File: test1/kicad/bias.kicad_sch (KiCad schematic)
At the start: 12 parts, among them Q40 PMZ1200UPEYL, Q41 PMZ1200UPEYL, Q42 2N7002 DNP, Q43 2N7002 DNP, U40 MCP4728, U41 OPA2388

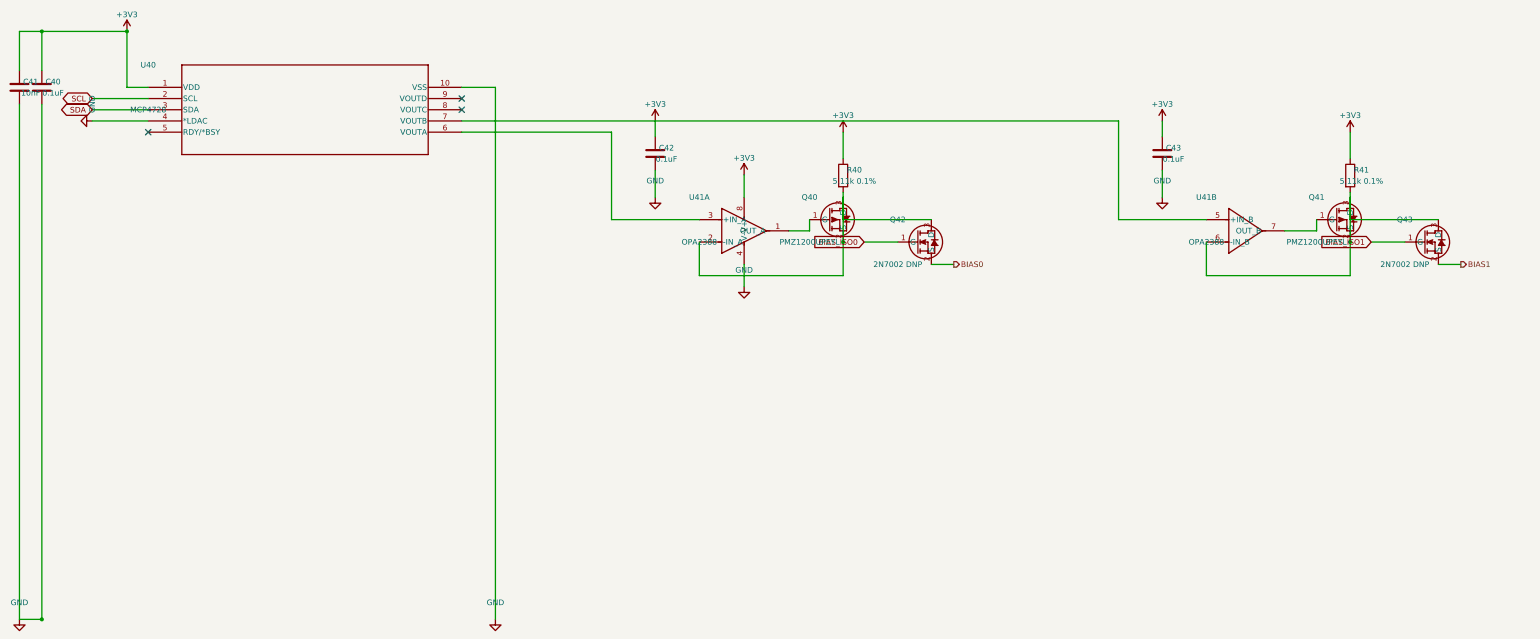
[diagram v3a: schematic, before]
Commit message: Split test1 generator into per-sheet package with netlist YAML + strict validator
Combines three layered changes:

1. Apply the design-review audit (test1/error_log.md): 9 ERRORs + 10
   WARNINGs from the new .claude/skills/design_review.md skill — FMC
   LA-bank 0Ω routing, Bobcat SPI/control/GPIO pull network, LDO
   ANY-OUT to FPGA, LDO_PG pull-up + series, bias DNP convention,
   kelvin SNS, per-pin VDDIO + bulk caps, BIAS bypass, VADJ/VDDIO bulk,
   MCP4728 EEPROM provisioning notes, shared-rail decision documented.

2. Refactor test1/gen_schematic.py (1825 lines → 138-line entry point)
   into a per-sheet package at test1/gen/:
     config.py / symbols.py / shared.py  — primitives, Sheet container,
     LA_ASSIGN, footprints, sexpr emit
     build_<sheet>.py × 7                — one builder per child sheet
     netlist.py / validator.py           — YAML loader + strict checker
   Per-session context for any single sheet drops to ~500 lines.
   Also sorts non-deterministic set iteration that made fmc.kicad_sch
   diff noisily across runs.

3. Add a declarative connectivity layer (netlist/<sheet>.yaml):
   parts inventory + nets (power / hier / global / internal), with
   explicit unit syntax for multi-unit symbols (U41:u2.7, J3:u3.G16).
   The strict validator runs at the end of every build_<sheet>() call:
     - inventory: YAML parts ↔ placed (refdes, unit) parity
     - connectivity: every YAML net member is in a connected component
       named the YAML net name (Union-Find on wires + junctions + label
       anchors + power-symbol pins; T-intersections auto-connect)
     - internal nets: members in one component, no name check
   Sheet now records structured PlacedPart/wire/label data alongside
   the s-expr emit; validator reads those instead of re-parsing.

All 6 child sheets' .kicad_sch outputs are byte-identical to the
post-design-review reference, and verify_project.py reports 0 issues.

Co-Authored-By: Claude Opus 4.7 (1M context) <noreply@anthropic.c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
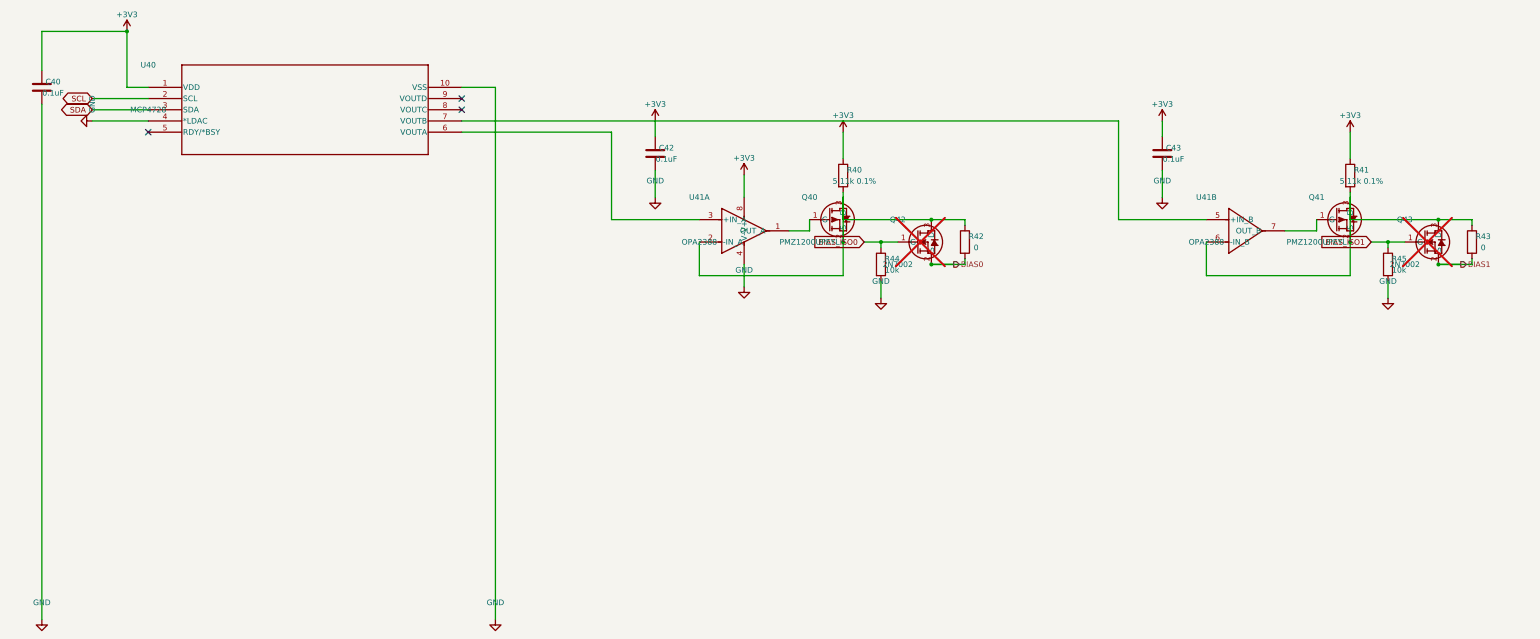
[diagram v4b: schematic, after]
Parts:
- removed C41: 10nF, Capacitor_SMD:C_0402_1005Metric, symbol Device:C
- added R42, R43: 0, Resistor_SMD:R_0402_1005Metric, symbol Device:R
- added R44, R45: 10k, Resistor_SMD:R_0402_1005Metric, symbol Device:R
- Q42, Q43: value 2N7002 DNP -> 2N7002; now not fitted
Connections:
- net BIAS0: now also R42.2
- net BIAS1: now also R43.2
- net BIAS_ISO0: now also R44.1
- net BIAS_ISO1: now also R45.1
- net GND: now also R44.2, R45.2
- net at Q41.2 (S), Q41.3 (D), Q43.3 (D)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: now also R43.1
- net at Q40.2 (S), Q40.3 (D), Q42.3 (D)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: now also R42.1
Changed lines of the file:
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@@
   (wire (pts (xy 55.88 83.81) (xy 55.88 200.66)) (stroke (width 0) (type default)))
   (symbol
-    (lib_id "Device:C")
-    (at 50.8 80 0)
-    (unit 1) (in_bom yes) (on_board yes) (dnp no)
-    (property "Reference" "C41" (at 53.339999999999996 78.73 0) (effects (font (size 1.27 1.27))))
-    (property "Value" "10nF" (at 53.339999999999996 81.27 0) (effects (font (size 1.27 1.27))))
-    (property "Footprint" "Capacitor_SMD:C_0402_1005Metric" (at 0 0 0) (effects (font (size 1.27 1.27)) (hide yes)))
-    (property "Datasheet" "" (at 0 0 0) (effects (font (size 1.27 1.27)) (hide yes)))
-    (pin "1")
-    (pin "2")
-    (instances
-      (project "test1"
-        (path "/4ed7a046-ef33-57d9-8730-321c05965af3/ddf1c49f-55ac-530a-9ee4-38ad9d14caf8" (reference "C41") (unit 1)))))
-  (wire (pts (xy 50.8 76.19) (xy 50.8 67.31)) (stroke (width 0) (type default)))
-  (wire (pts (xy 50.8 67.31) (xy 55.88 67.31)) (stroke (width 0) (type default)))
-  (junction (at 55.88 67.31) (diameter 0) (color 0 0 0 0))
-  (wire (pts (xy 50.8 83.81) (xy 50.8 200.66)) (stroke (width 0) (type default)))
-  (wire (pts (xy 50.8 200.66) (xy 55.88 200.66)) (stroke (width 0) (type default)))
-  (junction (at 55.88 200.66) (diameter 0) (color 0 0 0 0))
-  (symbol
-    (lib_id "power:GND")
-    (at 50.8 200.66 0)
-    (unit 1) (in_bom yes) (on_board yes) (dnp no)
-    (property "Reference" "#PWRa06f21d9" (at 50.8 194.31 0) (effects (font (size 1.27 1.27)) (hide yes)))
-    (property "Value" "GND" (at 50.8 196.85 0) (effects (font (size 1.27 1.27))))
-    (property "Footprint" "" (at 0 0 0) (effects (font (size 1.27 1.27)) (hide yes)))
-    (property "Datasheet" "" (at 0 0 0) (effects (font (size 1.27 1.27)) (hide yes)))
-    (pin "1")
-    (instances
-      (project "test1"
-        (path "/4ed7a046-ef33-57d9-8730-321c05965af3/ddf1c49f-55ac-530a-9ee4-38ad9d14caf8" (reference "#PWRa06f21d9") (unit 1)))))
+    (lib_id "power:GND")
+    (at 55.88 200.66 0)
+    (unit 1) (in_bom yes) (on_board yes) (dnp no)
+    (property "Reference" "#PWR807a04e0" (at 55.88 194.31 0) (effects (font (size 1.27 1.27)) (hide yes)))
+    (property "Value" "GND" (at 55.88 196.85 0) (effects (font (size 1.27 1.27))))
+    (property "Footprint" "" (at 0 0 0) (effects (font (size 1.27 1.27)) (hide yes)))
+    (property "Datasheet" "" (at 0 0 0) (effects (font (size 1.27 1.27)) (hide yes)))
+    (pin "1")
+    (instances
+      (project "test1"
+        (path "/4ed7a046-ef33-57d9-8730-321c05965af3/ddf1c49f-55ac-530a-9ee4-38ad9d14caf8" (reference "#PWR807a04e0") (unit 1)))))
   (symbol
     (lib_id "Lib:OPA2388")
@@
     (lib_id "Lib:2N7002")
     (at 250 115.08 0)
-    (unit 1) (in_bom yes) (on_board yes) (dnp no)
+    (unit 1) (in_bom yes) (on_board yes) (dnp yes)
     (property "Reference" "Q42" (at 250 110.0 0) (effects (font (size 1.27 1.27))))
-    (property "Value" "2N7002 DNP" (at 250 120.16 0) (effects (font (size 1.27 1.27))))
+    (property "Value" "2N7002" (at 250 120.16 0) (effects (font (size 1.27 1.27))))
     (property "Footprint" "Package_TO_SOT_SMD:SOT-23" (at 0 0 0) (effects (font (size 1.27 1.27)) (hide yes)))
     (property "Datasheet" "" (at 0 0 0) (effects (font (size 1.27 1.27)) (hide yes)))
@@
   (wire (pts (xy 250.0 115.08) (xy 242.38 115.08)) (stroke (width 0) (type default)))
   (global_label "BIAS_ISO0" (shape input) (at 242.38 115.08 180) (effects (font (size 1.27 1.27)) (justify right)))
+  (symbol
+    (lib_id "Device:R")
+    (at 265.24 115.08 0)
+    (unit 1) (in_bom yes) (on_board yes) (dnp no)
+    (property "Reference" "R42" (at 267.78000000000003 113.81 0) (effects (font (size 1.27 1.27))))
+    (property "Value" "0" (at 267.78000000000003 116.35 0) (effects (font (size 1.27 1.27))))
+    (property "Footprint" "Resistor_SMD:R_0402_1005Metric" (at 0 0 0) (effects (font (size 1.27 1.27)) (hide yes)))
+    (property "Datasheet" "" (at 0 0 0) (effects (font (size 1.27 1.27)) (hide yes)))
+    (pin "1")
+    (pin "2")
+    (instances
+      (project "test1"
+        (path "/4ed7a046-ef33-57d9-8730-321c05965af3/ddf1c49f-55ac-530a-9ee4-38ad9d14caf8" (reference "R42") (unit 1)))))
+  (junction (at 257.62 110.0) (diameter 0) (color 0 0 0 0))
+  (wire (pts (xy 257.62 110.0) (xy 265.24 110.0)) (stroke (width 0) (type default)))
+  (wire (pts (xy 265.24 110.0) (xy 265.24 111.27)) (stroke (width 0) (type default)))
+  (junction (at 257.62 120.16) (diameter 0) (color 0 0 0 0))
+  (wire (pts (xy 257.62 120.16) (xy 265.24 120.16)) (stroke (width 0) (type default)))
+  (wire (pts (xy 265.24 120.16) (xy 265.24 118.89)) (stroke (width 0) (type default)))
+  (junction (at 246.19 115.08) (diameter 0) (color 0 0 0 0))
+  (symbol
+    (lib_id "Device:R")
+    (at 246.19 120.16 0)
+    (unit 1) (in_bom yes) (on_board yes) (dnp no)
+    (property "Reference" "R44" (at 248.73 118.89 0) (effects (font (size 1.27 1.27))))
+    (property "Value" "10k" (at 248.73 121.42999999999999 0) (effects (font (size 1.27 1.27))))
+    (property "Footprint" "Resistor_SMD:R_0402_1005Metric" (at 0 0 0) (effects (font (size 1.27 1.27)) (hide yes)))
+    (property "Datasheet" "" (at 0 0 0) (effects (font (size 1.27 1.27)) (hide yes)))
+    (pin "1")
+    (pin "2")
+    (instances
+      (project "test1"
+        (path "/4ed7a046-ef33-57d9-8730-321c05965af3/ddf1c49f-55ac-530a-9ee4-38ad9d14caf8" (reference "R44") (unit 1)))))
+  (wire (pts (xy 246.19 115.08) (xy 246.19 116.35)) (stroke (width 0) (type default)))
+  (wire (pts (xy 246.19 123.97) (xy 246.19 127.78)) (stroke (width 0) (type default)))
+  (symbol
+    (lib_id "power:GND")
+    (at 246.19 127.78 0)
+    (unit 1) (in_bom yes) (on_board yes) (dnp no)
+    (property "Reference" "#PWRe0ee7a24" (at 246.19 121.43 0) (effects (font (size 1.27 1.27)) (hide yes)))
+    (property "Value" "GND" (at 246.19 123.97 0) (effects (font (size 1.27 1.27))))
+    (property "Footprint" "" (at 0 0 0) (effects (font (size 1.27 1.27)) (hide yes)))
+    (property "Datasheet" "" (at 0 0 0) (effects (font (size 1.27 1.27)) (hide yes)))
+    (pin "1")
+    (instances
+      (project "test1"
+        (path "/4ed7a046-ef33-57d9-8730-321c05965af3/ddf1c49f-55ac-530a-9ee4-38ad9d14caf8" (reference "#PWRe0ee7a24") (unit 1)))))
   (wire (pts (xy 215.16 104.92) (xy 215.16 99.84)) (stroke (width 0) (type default)))
   (symbol
@@
     (lib_id "Lib:2N7002")
     (at 365 115.08 0)
-    (unit 1) (in_bom yes) (on_board yes) (dnp no)
+    (unit 1) (in_bom yes) (on_board yes) (dnp yes)
     (property "Reference" "Q43" (at 365 110.0 0) (effects (font (size 1.27 1.27))))
-    (property "Value" "2N7002 DNP" (at 365 120.16 0) (effects (font (size 1.27 1.27))))
+    (property "Value" "2N7002" (at 365 120.16 0) (effects (font (size 1.27 1.27))))
     (property "Footprint" "Package_TO_SOT_SMD:SOT-23" (at 0 0 0) (effects (font (size 1.27 1.27)) (hide yes)))
     (property "Datasheet" "" (at 0 0 0) (effects (font (size 1.27 1.27)) (hide yes)))
@@
   (global_label "BIAS_ISO1" (shape input) (at 357.38 115.08 180) (effects (font (size 1.27 1.27)) (justify right)))
   (symbol
+    (lib_id "Device:R")
+    (at 380.24 115.08 0)
+    (unit 1) (in_bom yes) (on_board yes) (dnp no)
+    (property "Reference" "R43" (at 382.78000000000003 113.81 0) (effects (font (size 1.27 1.27))))
+    (property "Value" "0" (at 382.78000000000003 116.35 0) (effects (font (size 1.27 1.27))))
+    (property "Footprint" "Resistor_SMD:R_0402_1005Metric" (at 0 0 0) (effects (font (size 1.27 1.27)) (hide yes)))
+    (property "Datasheet" "" (at 0 0 0) (effects (font (size 1.27 1.27)) (hide yes)))
+    (pin "1")
+    (pin "2")
+    (instances
+      (project "test1"
+        (path "/4ed7a046-ef33-57d9-8730-321c05965af3/ddf1c49f-55ac-530a-9ee4-38ad9d14caf8" (reference "R43") (unit 1)))))
+  (junction (at 372.62 110.0) (diameter 0) (color 0 0 0 0))
+  (wire (pts (xy 372.62 110.0) (xy 380.24 110.0)) (stroke (width 0) (type default)))
+  (wire (pts (xy 380.24 110.0) (xy 380.24 111.27)) (stroke (width 0) (type default)))
+  (junction (at 372.62 120.16) (diameter 0) (color 0 0 0 0))
+  (wire (pts (xy 372.62 120.16) (xy 380.24 120.16)) (stroke (width 0) (type default)))
+  (wire (pts (xy 380.24 120.16) (xy 380.24 118.89)) (stroke (width 0) (type default)))
+  (junction (at 361.19 115.08) (diameter 0) (color 0 0 0 0))
+  (symbol
+    (lib_id "Device:R")
+    (at 361.19 120.16 0)
+    (unit 1) (in_bom yes) (on_board yes) (dnp no)
+    (property "Reference" "R45" (at 363.73 118.89 0) (effects (font (size 1.27 1.27))))
+    (property "Value" "10k" (at 363.73 121.42999999999999 0) (effects (font (size 1.27 1.27))))
+    (property "Footprint" "Resistor_SMD:R_0402_1005Metric" (at 0 0 0) (effects (font (size 1.27 1.27)) (hide yes)))
+    (property "Datasheet" "" (at 0 0 0) (effects (font (size 1.27 1.27)) (hide yes)))
+    (pin "1")
+    (pin "2")
+    (instances
+      (project "test1"
+        (path "/4ed7a046-ef33-57d9-8730-321c05965af3/ddf1c49f-55ac-530a-9ee4-38ad9d14caf8" (reference "R45") (unit 1)))))
+  (wire (pts (xy 361.19 115.08) (xy 361.19 116.35)) (stroke (width 0) (type default)))
+  (wire (pts (xy 361.19 123.97) (xy 361.19 127.78)) (stroke (width 0) (type default)))
+  (symbol
+    (lib_id "power:GND")
+    (at 361.19 127.78 0)
+    (unit 1) (in_bom yes) (on_board yes) (dnp no)
+    (property "Reference" "#PWRad49c2e3" (at 361.19 121.43 0) (effects (font (size 1.27 1.27)) (hide yes)))
+    (property "Value" "GND" (at 361.19 123.97 0) (effects (font (size 1.27 1.27))))
+    (property "Footprint" "" (at 0 0 0) (effects (font (size 1.27 1.27)) (hide yes)))
+    (property "Datasheet" "" (at 0 0 0) (effects (font (size 1.27 1.27)) (hide yes)))
+    (pin "1")
+    (instances
+      (project "test1"
+        (path "/4ed7a046-ef33-57d9-8730-321c05965af3/ddf1c49f-55ac-530a-9ee4-38ad9d14caf8" (reference "#PWRad49c2e3") (unit 1)))))
+  (symbol
     (lib_id "Device:C")
